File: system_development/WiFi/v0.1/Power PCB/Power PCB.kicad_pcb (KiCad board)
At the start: 2 copper layers, 30.5 x 53.3 mm, 14 parts, among them J1 Barrel_Jack, SW1 SW_DIP_x01, U1 LF15_TO252, U2 INA219A

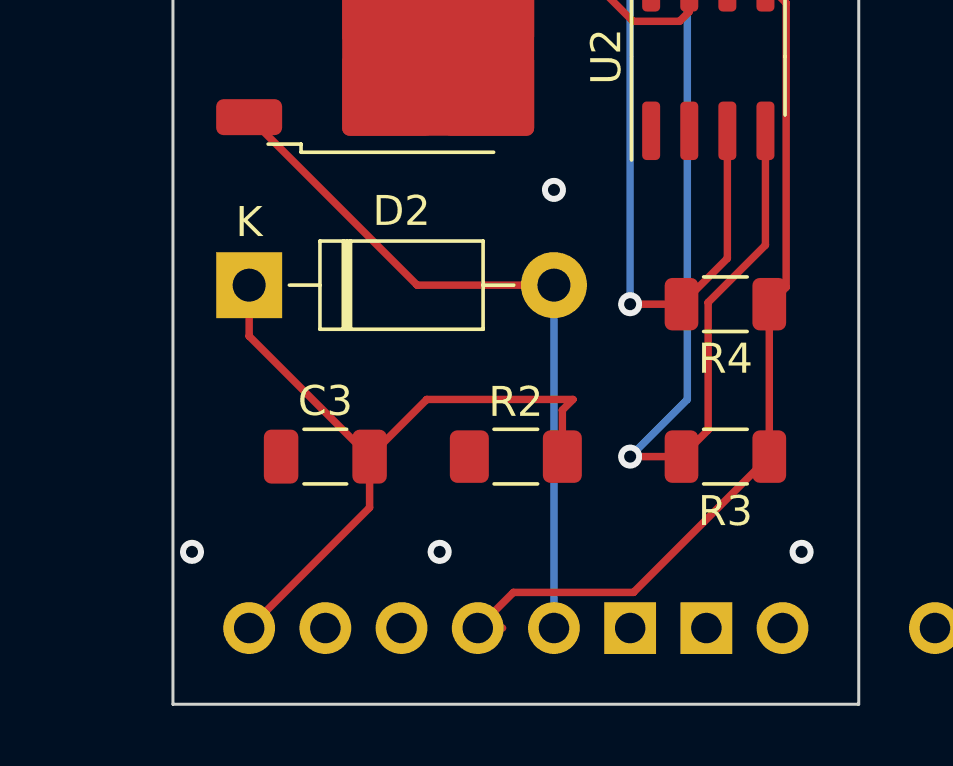
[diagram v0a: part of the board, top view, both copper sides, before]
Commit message: Redid PCB's for Wifi Version
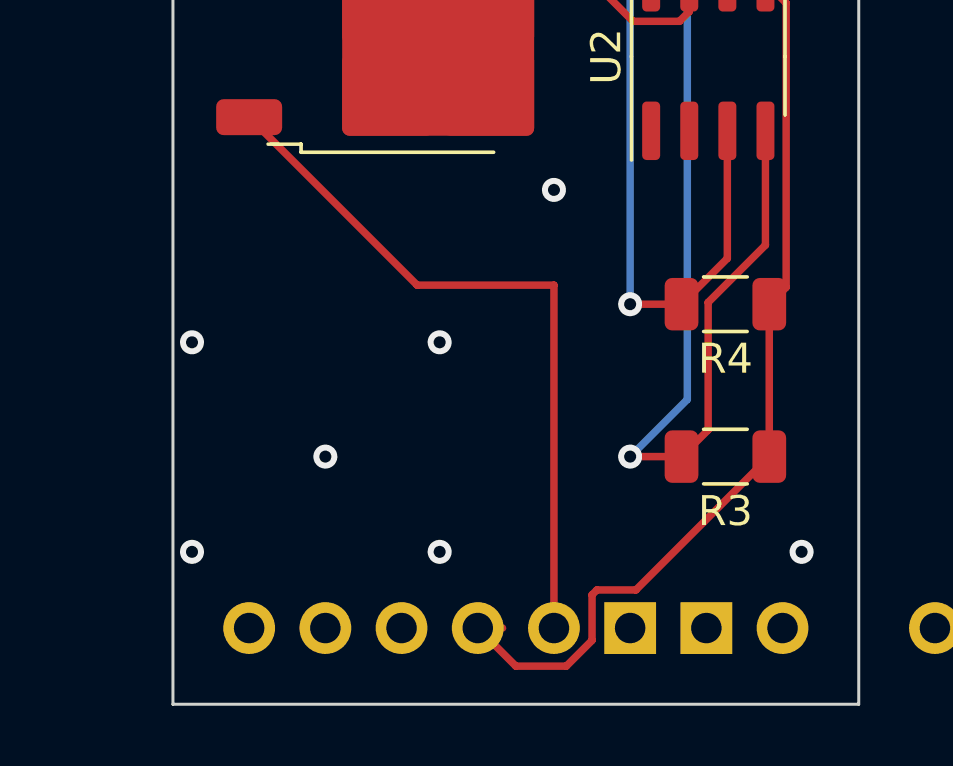
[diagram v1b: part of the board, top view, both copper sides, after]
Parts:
- removed C3: 22 μF, Capacitor_SMD:C_1206_3216Metric
- removed D2: 1N4005, Diode_THT:D_DO-41_SOD81_P10.16mm_Horizontal
- removed R2: 510, Resistor_SMD:R_1206_3216Metric_Pad1.30x1.75mm_HandSolder
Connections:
- XA1 pad VBAT: Net-(D2-K) -> unconnected-(XA1-PadVBAT)
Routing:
- net Net-(D2-K): track 24.4 -> 0.00 mm
- net Net-(U2-VS): track 29.2 -> 31.2 mm
- net GND: vias 8 -> 11
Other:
- board text added: "Nicholas Liger 06/21/24 ARTS Lab - USC Wifi Power Board v0.1"
- board text removed: "Nicholas Liger 06/18/24 ARTS Lab - USC Power Board v0.21"
